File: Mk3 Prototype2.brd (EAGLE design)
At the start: 119.6 x 68 mm, 138 parts, among them IC1 TPD3E001DRL, IC2 TPS62082, IC3 STM32F401V, IC6 CC3100MOD, IC7 BQ2970, J1 ZX62-AB-5PA(11), J2 ER-TFT024-3, J3 SWD_SHROUD, Q1 DMMT5401, Q2 NTR4101, Q6 NTR4101, SW1 JOYSTICK_MINI_MULTICOMP, U3 MCP73831, U4 USD-SOCKETNEW, X2 16MHz-3.2-2.5, X3 ABS07-32.768KHZ-T

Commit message: more part specing
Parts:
- L1: value (none) -> SRN2512-2R2M
- LED1, R1: value (none) -> DNP
- LED2, LED4, LED5: value (none) -> RED
- LED3: value (none) -> GREEN
- Q2, Q6: device TiLDA Mk3 Parts:SOT23-R -> TiLDA Mk3 Parts:Q3A
- Q3, Q8: value (none) -> CSD13202Q2; device TiLDA Mk3 Parts:SOT23-3 -> TiLDA Mk3 Parts:Q2
- R10: value 0603/1k/5% -> 0603/2k/5%
- R12: value (none) -> 0603/150/5%
- R14: value (none) -> 0603/120/5%
- R2: value (none) -> 0603/330/5%
- R20: value 0603/100K/5% -> 0603/220k/5%
- R43: value 0603/220/5% -> 0603/150/5%
- R51: value 330 -> 0603/330/5%
- S3, S4: value SWITCH-MOMENTARY-2 -> 1217769
- S8: value SWITCH-MOMENTARY-2SMD-1101NE -> DNP
- moved Q3 0.40 mm to (11.2, 52.0), turned to 180 degrees
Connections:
- net GND: now also Q3.4, Q3.EP2, Q8.4, Q8.EP2; no longer Q3.2, Q8.2
- net N$14: now also Q3.1, Q3.2, Q3.5, Q3.6, Q3.EP1; no longer Q3.3
- net N$15: now also Q2.5, Q2.6, Q2.7, Q2.8, Q2.EP, Q6.5, Q6.6, Q6.7, Q6.8, Q6.EP; no longer Q2.2, Q6.2
- net N$54: now also Q6.4; no longer Q6.1
- net N$6: now also Q2.4; no longer Q2.1
- net N$64: now also Q8.1, Q8.2, Q8.5, Q8.6, Q8.EP1; no longer Q8.3
- net TIM1_CH1N: now also Q3.3; no longer Q3.1
- net TIM4_CH4: now also Q8.3; no longer Q8.1
- net VBAT: now also Q2.1, Q2.2
- net V_UNREG: now also Q6.1, Q6.2
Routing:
- net N$15: track 20.6 -> 29.4 mm
- net N$6: track 3.52 -> 6.35 mm
- net VBAT: track 79.8 -> 82.3 mm
- net GND: track 127.1 -> 129.0 mm
- net V_UNREG: track 62.4 -> 64.0 mm
- net TIM4_CH4: track 114.3 -> 115.8 mm
- net N$54: track 19.4 -> 20.6 mm

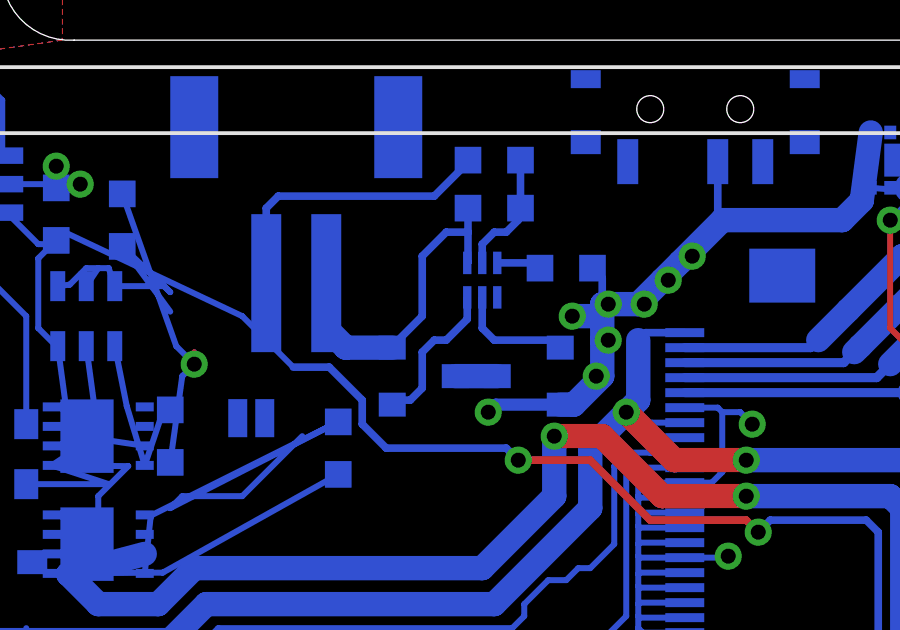
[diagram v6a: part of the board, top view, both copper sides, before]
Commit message: changing mosfet part
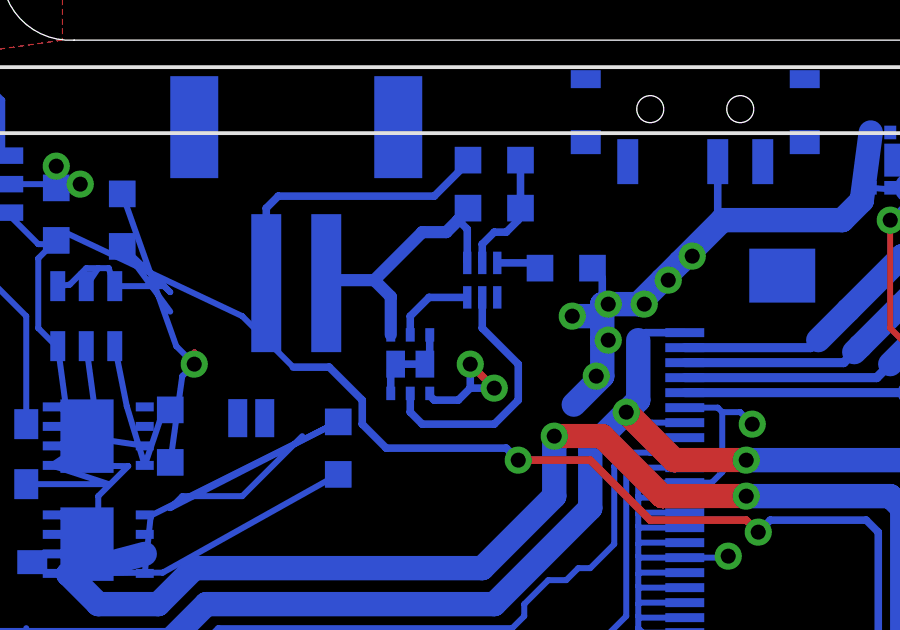
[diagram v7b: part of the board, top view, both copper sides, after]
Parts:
- removed Q7: (no value), TiLDA Mk3 Parts:SOT23-3
- Q2, Q6: value NTR4101 -> (none)
- Q4: value (none) -> CSD85301Q2; device TiLDA Mk3 Parts:SOT23-3 -> TiLDA Mk3 Parts:Q2_DUAL
- moved Q4 4.02 mm to (50.8, 52.4), turned to 180 degrees
- renumbered U3 to IC4
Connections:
- removed net N$45: Q4.3, Q7.3
- new net N$3: Q4.3, Q4.6, Q4.EP1, Q4.EP2
- net GND: now also Q4.4; no longer Q4.2
- net N$50: now also Q4.5; no longer Q4.1
- net N$55: now also Q4.2; no longer Q7.1
- net N$57: now also Q4.1; no longer Q7.2
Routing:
- net N$50: track 3.89 -> 8.64 mm
- net N$3: track 0.00 -> 3.06 mm
- net N$55: track 5.11 -> 2.78 mm
- net GND: track 129.0 -> 130.4 mm, vias 28 -> 29
- net N$45: track 1.40 -> 0.00 mm
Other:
- board text added: "Powered by:"

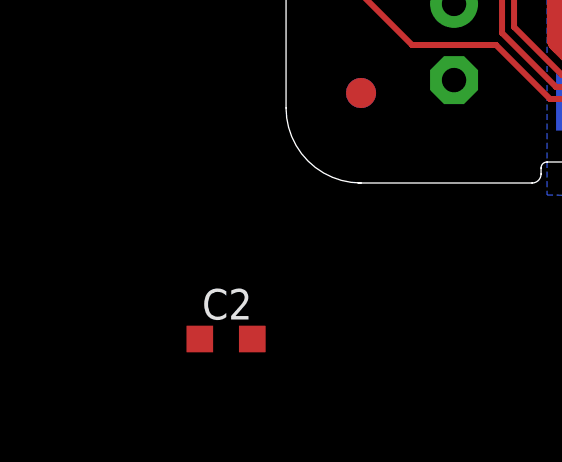
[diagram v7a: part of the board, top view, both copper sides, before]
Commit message: changed battery charger IC
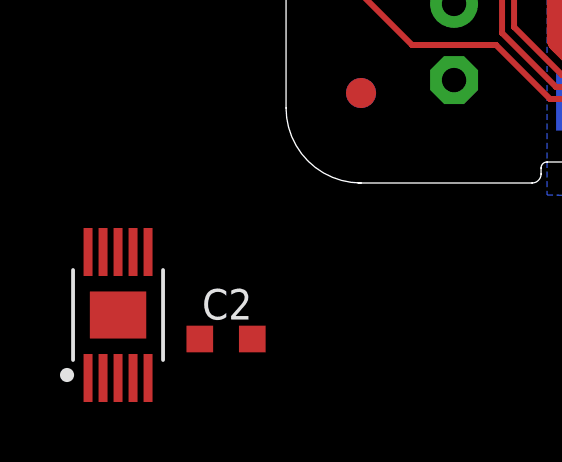
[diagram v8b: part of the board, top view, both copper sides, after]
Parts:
- added IC40: MCP73831, TiLDA Mk3 Parts:SOT23-5
- IC4: value MCP73831 -> BQ2409X; device TiLDA Mk3 Parts:SOT23-5 -> TiLDA Mk3 Parts:HVSSOP10
- moved IC4 75.3 mm to (-5.60, -4.40), flipped to the top, turned to 0 degrees
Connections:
- new net IN: IC4.1
- new net VSS: IC4.3, IC4.EP
- net CHARGING: now also IC40.1; no longer IC4.1
- net GND: now also IC40.2; no longer IC4.2
- net N$34: now also IC40.5; no longer IC4.5
- net VBAT: now also IC40.3; no longer IC4.3
- net VBUS: now also IC40.4; no longer IC4.4
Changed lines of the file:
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@@
 <attribute name="FARNELL" value="1217769" x="103.8" y="47.2" size="1.778" layer="27" rot="R90" display="off"/>
 </element>
-<element name="IC4" library="TiLDA Mk3 Parts" package="SOT23-5" value="MCP73831" x="36" y="58.4" smashed="yes" rot="MR270">
+<element name="IC40" library="TiLDA Mk3 Parts" package="SOT23-5" value="MCP73831" x="36" y="58.4" smashed="yes" rot="MR270">
 <attribute name="NAME" x="35.111" y="56.841" size="0.8128" layer="26" font="vector" ratio="14" rot="MR180"/>
 </element>
@@
 <element name="C27" library="passives-7351" package="C0805-N" value="0805/10u/10V/X5R" x="33.6" y="46.8" rot="MR0"/>
 <element name="Q4" library="TiLDA Mk3 Parts" package="Q2_DUAL" value="CSD85301Q2" x="50.8" y="52.4" rot="MR180"/>
+<element name="IC4" library="TiLDA Mk3 Parts" package="HVSSOP10" value="BQ2409X" x="-5.6" y="-4.4"/>
 </elements>
 <signals>
@@
 <contactref element="C21" pad="1"/>
 <contactref element="C20" pad="1"/>
-<contactref element="IC4" pad="2"/>
+<contactref element="IC40" pad="2"/>
 <contactref element="R6" pad="2"/>
 <contactref element="C3" pad="1"/>
@@
 </signal>
 <signal name="N$34">
-<contactref element="IC4" pad="5"/>
+<contactref element="IC40" pad="5"/>
 <contactref element="R6" pad="1"/>
 <wire x1="34.6999" y1="59.35" x2="34.6999" y2="60.5999" width="0.2" layer="16"/>
@@
 </signal>
 <signal name="VBAT">
-<contactref element="IC4" pad="3"/>
+<contactref element="IC40" pad="3"/>
 <contactref element="C3" pad="2"/>
 <contactref element="R21" pad="2"/>
@@
 <signal name="CHARGING">
 <contactref element="LED5" pad="C"/>
-<contactref element="IC4" pad="1"/>
+<contactref element="IC40" pad="1"/>
 <wire x1="23.25" y1="2.8" x2="8.8" y2="2.8" width="0.2" layer="1"/>
 <wire x1="8.8" y1="2.8" x2="7" y2="4.6" width="0.2" layer="1"/>
@@
 </signal>
 <signal name="VBUS">
-<contactref element="IC4" pad="4"/>
+<contactref element="IC40" pad="4"/>
 <contactref element="R2" pad="2"/>
 <contactref element="C1" pad="2"/>
@@
 <wire x1="50.15" y1="52.238" x2="50.312" y2="52.4" width="0.254" layer="16"/>
 </signal>
+<signal name="IN">
+<contactref element="IC4" pad="1"/>
+</signal>
+<signal name="VSS">
+<contactref element="IC4" pad="EP"/>
+<contactref element="IC4" pad="3"/>
+<wire x1="-5.6" y1="-4.4" x2="-5.6" y2="-6.5" width="0" layer="19" extent="1-1"/>
+</signal>
 </signals>
